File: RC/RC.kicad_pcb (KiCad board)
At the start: 2 copper layers, 95 x 90 mm, 45 parts, among them J1 BEC, J10 CJVL53L0XV2, J11 CJMCU-20948, J12 A3144 REMOTE, J2 ESP32L, J3 ESP32R, J4 BuckIn-, J5 BuckIn+, J6 BuckOut-, J7 BuckOut+, J8 VBAT_SENSE_IN, J9 3V3 LINK, M1 MG90

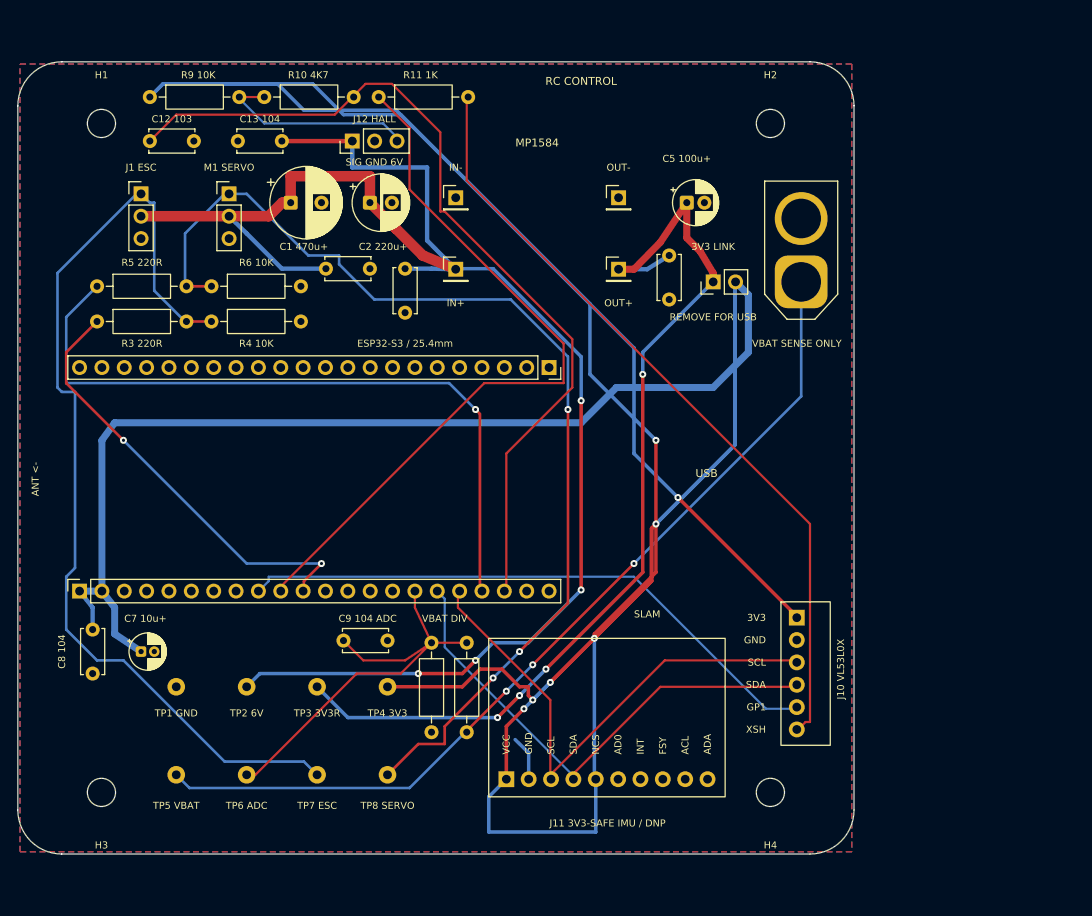
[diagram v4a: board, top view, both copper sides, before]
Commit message: Finalize 78x66 mm maximum-density RC carrier
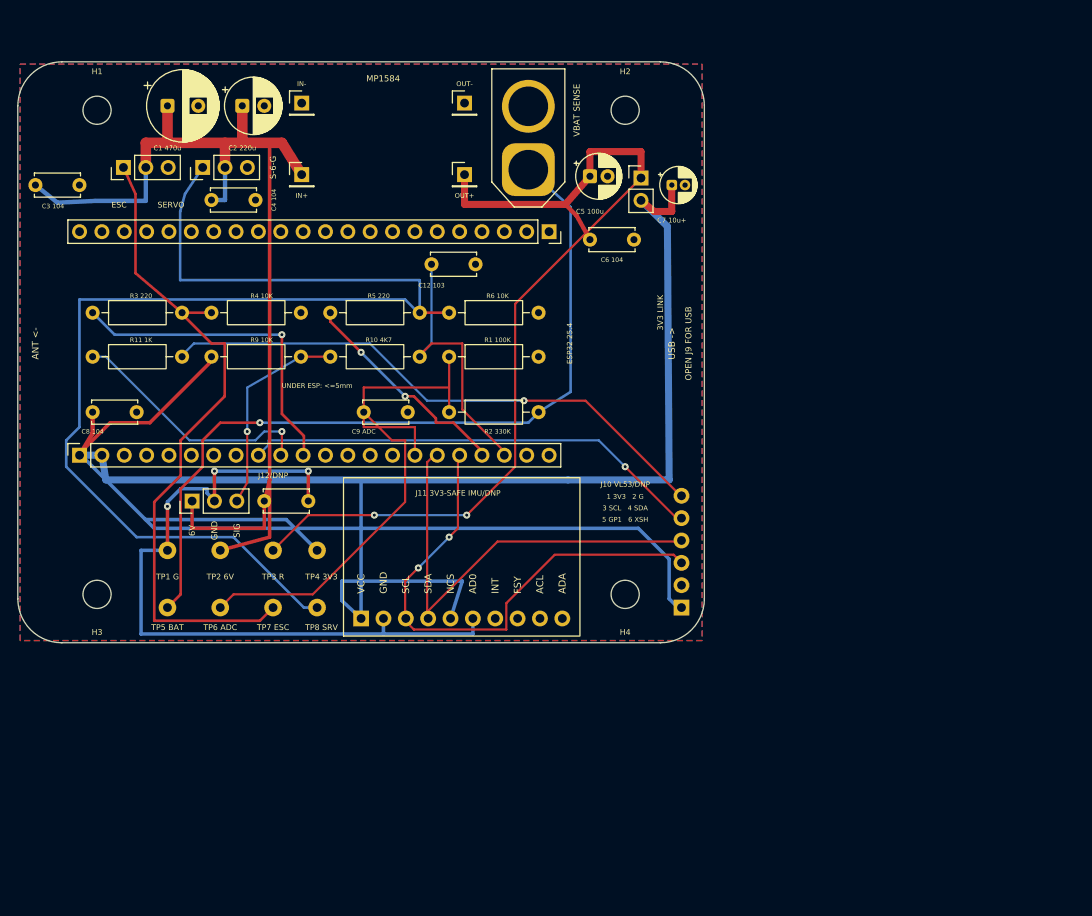
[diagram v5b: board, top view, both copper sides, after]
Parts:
- moved C7 80.3 mm to (94.3, 99.0)
- moved J12 44.8 mm to (39.8, 134.9)
- moved R11 43.9 mm to (28.5, 118.5)
- moved C13 40.9 mm to (48.0, 134.9), turned to 0 degrees
- moved C12 34.9 mm to (67.0, 108.0)
- moved C3 34.3 mm to (22.0, 99.0)
- moved J8 33.5 mm to (78.0, 97.2)
- moved R1 32.6 mm to (69.0, 118.5), turned to 0 degrees
- moved R10 30.4 mm to (55.5, 118.5)
- moved R9 30.3 mm to (42.0, 118.5)
- moved H4 27.9 mm to (89.0, 145.5)
- moved R6 27.2 mm to (69.0, 113.5)
- moved R5 26.7 mm to (55.5, 113.5)
- moved R2 26.3 mm to (69.0, 124.8), turned to 0 degrees
- moved C9 26.1 mm to (59.3, 124.8)
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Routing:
- net +3.3V: track 516.1 -> 273.2 mm, vias 7 -> 0
- net GND: track 5.15 -> 83.9 mm, vias 0 -> 3
- net /IO14: track 100.2 -> 31.9 mm
- net +6V: track 184.8 -> 123.5 mm, vias 4 -> 0
- net /PWM_SERVO: track 81.2 -> 25.1 mm, vias 1 -> 2
- net /IO17: track 83.4 -> 28.6 mm, vias 0 -> 1
- net /PWM_ESC_OUT: track 111.0 -> 78.1 mm
- net /VL_XSHUT: track 89.4 -> 65.3 mm, vias 0 -> 1
- net /PWM_SERVO_OUT: track 120.4 -> 141.8 mm, vias 3 -> 0
- net /VBAT_SENSE: track 49.0 -> 68.5 mm
- net /IO16: track 68.5 -> 53.1 mm, vias 0 -> 1
- net /PWM_ESC: track 49.9 -> 37.3 mm, vias 2 -> 1
- net /VBAT: track 103.4 -> 91.9 mm, vias 3 -> 1
- net /IO11: track 58.7 -> 51.9 mm
- net /BUCK_3V3_RAW: track 109.3 -> 105.8 mm, vias 4 -> 2
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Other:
- board size 95 x 90 mm -> 78 x 66 mm
- board text added: "1 3V3 2 G"
- board text added: "3 SCL 4 SDA"
- board text added: "5 GP1 6 XSH"
- board text added: "6V"
- board text added: "C1 470u"
- board text added: "C2 220u"
- board text added: "C3 104"
- board text added: "C4 104"
- board text added: "C5 100u"
- board text added: "C6 104"
- board text added: "C9 ADC"
- board text added: "ESC"
- board text added: "ESP32 25.4"
- board text added: "J10 VL53/DNP"
- board text added: "J11 3V3-SAFE IMU/DNP"
- board text added: "J12/DNP"
- board text added: "OPEN J9 FOR USB"
- board text added: "R1 100K"
- board text added: "R2 330K"
- board text added: "R3 220"
- board text added: "R5 220"
- board text added: "S-6-G"
- board text added: "SERVO"
- board text added: "SIG"
- board text added: "TP1 G"
- board text added: "TP3 R"
- board text added: "TP5 BAT"
- board text added: "TP8 SRV"
- board text added: "UNDER ESP: <=5mm"
- board text added: "USB ->"
- board text added: "VBAT SENSE"
- board text removed: "3V3"
- board text removed: "C1 470u+"
- board text removed: "C13 104"
- board text removed: "C2 220u+"
- board text removed: "C5 100u+"
- board text removed: "C9 104 ADC"
- board text removed: "ESP32-S3 / 25.4mm"
- board text removed: "GP1"
- board text removed: "J1 ESC"
- board text removed: "J10 VL53L0X"
- board text removed: "J11 3V3-SAFE IMU / DNP"
- board text removed: "J12 HALL"
- board text removed: "M1 SERVO"
- board text removed: "R3 220R"
- board text removed: "R5 220R"
- board text removed: "RC CONTROL"
- board text removed: "REMOVE FOR USB"
- board text removed: "SCL"
- board text removed: "SDA"
- board text removed: "SIG GND 6V"
- board text removed: "SLAM"
- board text removed: "TP1 GND"
- board text removed: "TP3 3V3R"
- board text removed: "TP5 VBAT"
- board text removed: "TP8 SERVO"
- board text removed: "USB"
- board text removed: "VBAT DIV"
- board text removed: "VBAT SENSE ONLY"
- board text removed: "XSH"

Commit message: Finalize 74x66 mm RC carrier after physical fit verification
Reduce the carrier width from 78 mm to 74 mm while preserving circuit topology and footprints. Relocate C3 and C7, reroute the compact layout, move permanent assembly legends to the bottom silkscreen, and retain critical top-side safety labels.

ESP32-S3 and MP1584 footprints were verified with a 1:1 physical fit check.
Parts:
- moved C7 10.5 mm to (94.0, 109.5)
- moved C3 8.91 mm to (30.8, 100.7), turned to 180 degrees
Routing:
- net +6V: track 123.5 -> 113.0 mm
- net +3.3V: track 273.2 -> 266.3 mm
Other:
- board size 78 x 66 mm -> 74 x 66 mm
- board text added: "C13 104"
- board text added: "USB LOW <=7.5"

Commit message: Freeze 74x66 mm RC carrier for fabrication
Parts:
- moved C7 3.01 mm to (94.2, 106.5)
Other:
- board text added: "J10 VL53L0X"
- board text added: "J11 3v3 IMU"
- board text added: "J12"
- board text removed: "1 3V3 2 G"
- board text removed: "3 SCL 4 SDA"
- board text removed: "5 GP1 6 XSH"
- board text removed: "J10 VL53/DNP"
- board text removed: "J11 3V3-SAFE IMU/DNP"
- board text removed: "J12/DNP"
- board text removed: "OPEN J9 FOR USB"
- board text removed: "USB LOW <=7.5"
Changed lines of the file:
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@@
 	(footprint "Capacitor_THT:CP_Radial_D4.0mm_P1.50mm"
 		(layer "F.Cu")
-		(at 94 109.5)
+		(at 94.25 106.5)
 		(descr "CP, Radial series, Radial, pin pitch=1.50mm, diameter=4mm, height=7mm, Electrolytic Capacitor")
 		(tags "CP Radial series Radial pin pitch 1.50mm diameter 4mm height 7mm Electrolytic Capacitor")
@@
 			(layer "F.Fab")
 		)
-		(fp_text user "J10 VL53L0X"
-			(at 2.1 -6.5 270)
-			(layer "F.Fab")
+		(fp_text user "XSHUT"
+			(at 1.9 12.75 180)
+			(layer "F.SilkS")
 			(effects
 				(font
@@
 					(thickness 0.13)
 				)
+				(justify right)
 			)
 		)
-		(fp_text user "XSHUT / IO17"
-			(at -3 12.7 180)
-			(layer "F.Fab")
+		(fp_text user "GPIO1"
+			(at 1.9 10.25 180)
+			(layer "F.SilkS")
 			(effects
 				(font
@@
 			)
 		)
-		(fp_text user "GPIO1 / IO16"
-			(at -3 10.16 180)
-			(layer "F.Fab")
+		(fp_text user "SDA"
+			(at 1.9 7.62 180)
+			(layer "F.SilkS")
 			(effects
 				(font
@@
 			)
 		)
-		(fp_text user "SDA / IO11"
-			(at -3 7.62 180)
-			(layer "F.Fab")
+		(fp_text user "SCL"
+			(at 1.9 5.08 180)
+			(layer "F.SilkS")
 			(effects
 				(font
@@
 			)
 		)
-		(fp_text user "SCL / IO12"
-			(at -3 5.08 180)
-			(layer "F.Fab")
+		(fp_text user "GND"
+			(at 1.65 2.5 180)
+			(layer "F.SilkS")
 			(effects
 				(font
@@
 			)
 		)
-		(fp_text user "GND"
-			(at -3 2.54 180)
-			(layer "F.Fab")
+		(fp_text user "3V3"
+			(at 1.65 0 180)
+			(layer "F.SilkS")
 			(effects
 				(font
@@
 			)
 		)
-		(fp_text user "3V3"
-			(at -3 0 180)
+		(fp_text user "J10 VL53L0X"
+			(at 2.1 -6.5 270)
 			(layer "F.Fab")
 			(effects
@@
 					(thickness 0.13)
 				)
-				(justify right)
 			)
 		)
@@
 		(layer "Edge.Cuts")
 	)
-	(gr_text "UNDER ESP: <=5mm"
-		(at 54 121.8 0)
+	(gr_text "IN-"
+		(at 52.25 87.5 0)
 		(layer "F.SilkS")
 		(effects
@@
 		)
 	)
-	(gr_text "1 3V3   2 G"
-		(at 89 134.4 0)
+	(gr_text "IN+"
+		(at 52.25 100.2 0)
 		(layer "F.SilkS")
 		(effects
@@
 		)
 	)
-	(gr_text "3 SCL   4 SDA"
-		(at 89 135.7 0)
+	(gr_text "UNDER ESP: <=5mm"
+		(at 54 121.8 0)
 		(layer "F.SilkS")
 		(effects
@@
 		)
 	)
-	(gr_text "5 GP1   6 XSH"
-		(at 89 137 0)
+	(gr_text "OUT-"
+		(at 70.75 87.5 0)
 		(layer "F.SilkS")
 		(effects
@@
 		)
 	)
-	(gr_text "USB LOW <=7.5"
-		(at 90.5 120 90)
+	(gr_text "OUT+"
+		(at 70.75 100.2 0)
 		(layer "F.SilkS")
 		(effects
@@
 		)
 	)
-	(gr_text "J10 VL53/DNP"
-		(at 89 133 0)
+	(gr_text "J10 VL53L0X"
+		(at 93.75 131.75 0)
 		(layer "F.SilkS")
 		(effects
@@
 		)
 	)
-	(gr_text "J12/DNP"
+	(gr_text "J12"
 		(at 49 132 0)
 		(layer "F.SilkS")
@@
 		)
 	)
-	(gr_text "J11 3V3-SAFE IMU/DNP"
+	(gr_text "J11 3v3 IMU"
 		(at 70 134 0)
 		(layer "F.SilkS")
@@
 		)
 	)
+	(gr_text "MP1584"
+		(at 61.5 86.9 0)
+		(layer "F.SilkS")
+		(effects
+			(font
+				(size 0.7 0.7)
+				(thickness 0.15)
+			)
+		)
+	)
 	(gr_text "6V"
 		(at 39.8 138.25 90)
@@
 		)
 	)
-	(gr_text "OPEN J9 FOR USB"
-		(at 96.2 117 90)
-		(layer "F.SilkS")
-		(effects
-			(font
-				(size 0.7 0.7)
-				(thickness 0.15)
-			)
-		)
-	)
 	(gr_text "USB ->"
 		(at 94.5 118.25 90)
@@
 		)
 	)
-	(gr_text "IN-"
-		(at 52.25 87.5 0)
-		(layer "B.SilkS")
-		(effects
-			(font
-				(size 0.55 0.55)
-				(thickness 0.13)
-			)
-			(justify mirror)
-		)
-	)
-	(gr_text "IN+"
-		(at 52.25 100.2 0)
-		(layer "B.SilkS")
-		(effects
-			(font
-				(size 0.55 0.55)
-				(thickness 0.13)
-			)
-			(justify mirror)
-		)
-	)
-	(gr_text "OUT-"
-		(at 70.75 87.5 0)
-		(layer "B.SilkS")
-		(effects
-			(font
-				(size 0.55 0.55)
-				(thickness 0.13)
-			)
-			(justify mirror)
-		)
-	)
-	(gr_text "OUT+"
-		(at 70.75 100.2 0)
-		(layer "B.SilkS")
-		(effects
-			(font
-				(size 0.55 0.55)
-				(thickness 0.13)
-			)
-			(justify mirror)
-		)
-	)
 	(gr_text "C5 100u"
 		(at 85 102 0)
@@
 			)
 			(justify mirror)
-		)
-	)
-	(gr_text "MP1584"
-		(at 61.5 86.9 0)
-		(layer "B.SilkS")
-		(effects
-			(font
-				(size 0.7 0.7)
-				(thickness 0.15)
-			)
-			(justify mirror)

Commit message: Release RC carrier PCB v2.0 for fabrication
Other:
- board text added: "Damian's RC Car PCB"
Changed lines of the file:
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@@
 		(filling no)
 		(pcbplotparams
-			(layerselection 0x00000000_00000000_55555555_5755f5ff)
+			(layerselection 0x00000000_00000000_55555555_575555ff)
 			(plot_on_all_layers_selection 0x00000000_00000000_00000000_00000000)
 			(disableapertmacros no)
@@
 			(outputformat 1)
 			(mirror no)
-			(drillshape 1)
+			(drillshape 0)
 			(scaleselection 1)
-			(outputdirectory "")
+			(outputdirectory "C:/Users/Damia/Downloads/PCB/")
 		)
 	)
@@
 		)
 	)
+	(gr_text "Damian's\nRC Car PCB"
+		(at 24.5 138.5 0)
+		(layer "F.SilkS")
+		(effects
+			(font
+				(size 1 1)
+				(thickness 0.25)
+				(bold yes)
+			)
+			(justify left bottom)
+		)
+	)
